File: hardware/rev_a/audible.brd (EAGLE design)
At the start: 27.7 x 23.4 mm, 28 parts, among them IC1 LTC1966CMS8, J1 SQUALL_HEADER, J5 TC2030-JLINK-NL, Q1 FK3503010L, U1 MAX417ESA+, U2 MAX417ESA+, U3 LD39015, U4 ICS-40310

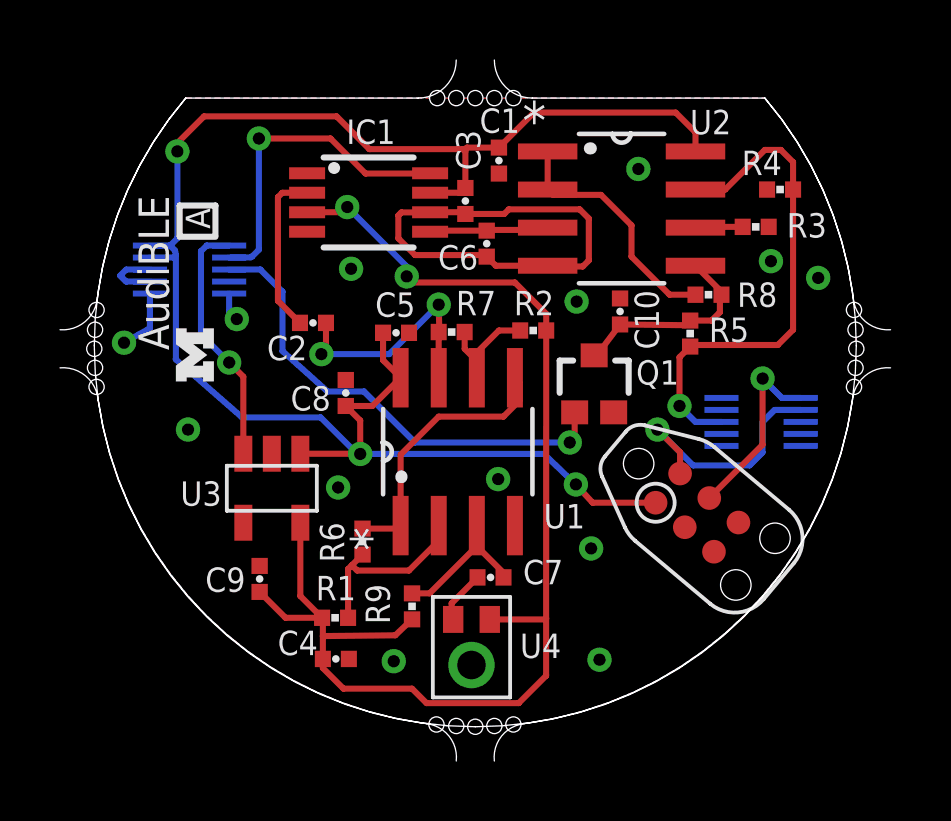
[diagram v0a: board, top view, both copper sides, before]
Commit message: Updated Part Names and digikey part names
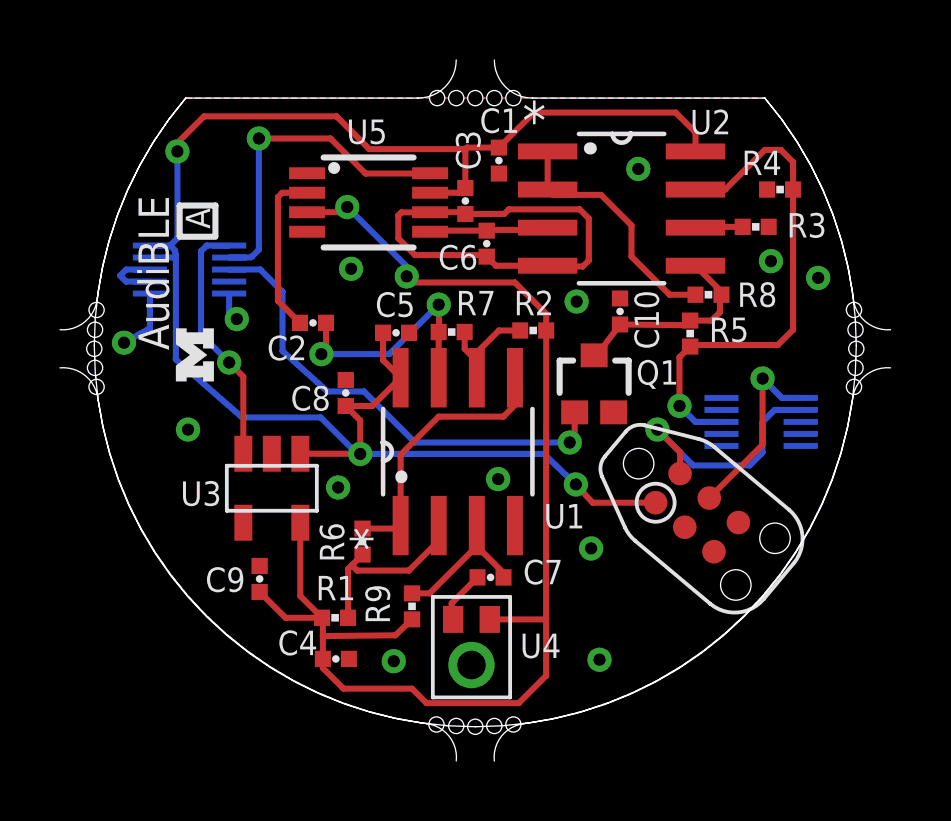
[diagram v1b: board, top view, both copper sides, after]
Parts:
- renumbered IC1 to U5, J5 to J2
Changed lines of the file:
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@@
 <grid distance="0.1" unitdist="mil" unit="mil" style="lines" multiple="1" display="yes" altdistance="0.01" altunitdist="inch" altunit="inch"/>
 <layers>
-<layer number="1" name="Top" color="4" fill="1" visible="no" active="yes"/>
+<layer number="1" name="Top" color="4" fill="1" visible="yes" active="yes"/>
 <layer number="2" name="Route2" color="1" fill="3" visible="no" active="no"/>
 <layer number="3" name="Route3" color="4" fill="3" visible="no" active="no"/>
@@
 <layer number="18" name="Vias" color="2" fill="1" visible="yes" active="yes"/>
 <layer number="19" name="Unrouted" color="13" fill="1" visible="yes" active="yes"/>
-<layer number="20" name="Dimension" color="15" fill="1" visible="no" active="yes"/>
-<layer number="21" name="tPlace" color="7" fill="1" visible="no" active="yes"/>
+<layer number="20" name="Dimension" color="15" fill="1" visible="yes" active="yes"/>
+<layer number="21" name="tPlace" color="7" fill="1" visible="yes" active="yes"/>
 <layer number="22" name="bPlace" color="7" fill="1" visible="yes" active="yes"/>
-<layer number="23" name="tOrigins" color="15" fill="1" visible="no" active="yes"/>
-<layer number="24" name="bOrigins" color="15" fill="1" visible="no" active="yes"/>
-<layer number="25" name="tNames" color="7" fill="1" visible="no" active="yes"/>
+<layer number="23" name="tOrigins" color="15" fill="1" visible="yes" active="yes"/>
+<layer number="24" name="bOrigins" color="15" fill="1" visible="yes" active="yes"/>
+<layer number="25" name="tNames" color="7" fill="1" visible="yes" active="yes"/>
 <layer number="26" name="bNames" color="7" fill="1" visible="yes" active="yes"/>
 <layer number="27" name="tValues" color="7" fill="1" visible="no" active="yes"/>
@@
 <layer number="49" name="Reference" color="7" fill="1" visible="no" active="yes"/>
 <layer number="50" name="dxf" color="7" fill="1" visible="no" active="no"/>
-<layer number="51" name="tDocu" color="6" fill="1" visible="no" active="yes"/>
-<layer number="52" name="bDocu" color="6" fill="1" visible="no" active="yes"/>
+<layer number="51" name="tDocu" color="6" fill="1" visible="yes" active="yes"/>
+<layer number="52" name="bDocu" color="6" fill="1" visible="yes" active="yes"/>
 <layer number="53" name="tGND_GNDA" color="7" fill="9" visible="no" active="no"/>
 <layer number="54" name="bGND_GNDA" color="1" fill="9" visible="no" active="no"/>
@@
 </element>
 <element name="U$1" library="logos" package="UMICH_SOLID_50MIL" value="" x="14.7828" y="12.3952" smashed="yes" rot="R90"/>
-<element name="J5" library="connector" package="TC2030-IDC-NL" value="TC2030-JLINK-NL" x="31.5214" y="7.1374" smashed="yes" rot="R320">
+<element name="J2" library="connector" package="TC2030-IDC-NL" value="TC2030-JLINK-NL" x="31.5214" y="7.1374" smashed="yes" rot="R320">
 <attribute name="VALUE" x="29.2764625" y="4.4619875" size="1.016" layer="27" font="vector" ratio="12" rot="R320" align="bottom-center"/>
 </element>
@@
 </element>
 <element name="U4" library="chips" package="LGA_CAV3" value="ICS-40310" x="24.003" y="2.0574" smashed="yes" rot="R270"/>
-<element name="IC1" library="chips" package="MSOP8" value="LTC1966CMS8" x="20.574" y="17.4752" smashed="yes" rot="R270">
+<element name="U5" library="chips" package="MSOP8" value="LTC1966CMS8" x="20.574" y="17.4752" smashed="yes" rot="R270">
 <attribute name="NAME" x="19.832" y="19.4278" size="0.8128" layer="25"/>
 <attribute name="VALUE" x="18.962" y="14.6472" size="1.016" layer="27"/>
@@
 <contactref element="J1" pad="A1"/>
 <contactref element="J1" pad="A3"/>
-<contactref element="J5" pad="1"/>
+<contactref element="J2" pad="1"/>
 <contactref element="C8" pad="1"/>
-<contactref element="IC1" pad="7"/>
+<contactref element="U5" pad="7"/>
 <contactref element="U1" pad="8"/>
 <contactref element="U2" pad="8"/>
@@
 <vertex x="33.782" y="20.955" curve="-40.54"/>
 </polygon>
-<contactref element="J5" pad="5"/>
+<contactref element="J2" pad="5"/>
 <contactref element="C8" pad="2"/>
 <contactref element="U2" pad="4"/>
-<contactref element="IC1" pad="1"/>
-<contactref element="IC1" pad="4"/>
+<contactref element="U5" pad="1"/>
+<contactref element="U5" pad="4"/>
 <contactref element="C9" pad="2"/>
 <contactref element="U4" pad="P$2"/>
@@
 <contactref element="C3" pad="1"/>
 <contactref element="C6" pad="1"/>
-<contactref element="IC1" pad="6"/>
+<contactref element="U5" pad="6"/>
 <wire x1="23.7998" y1="17.09293125" x2="25.09393125" y2="17.09293125" width="0.2032" layer="1"/>
 <wire x1="25.0698" y1="18.28673125" x2="24.9174" y2="18.43913125" width="0.2032" layer="1"/>
@@
 <signal name="P23">
 <contactref element="J1" pad="A4"/>
-<contactref element="IC1" pad="8"/>
+<contactref element="U5" pad="8"/>
 <via x="16.9164" y="19.6088" extent="1-16" drill="0.4064"/>
 <wire x1="16.9164" y1="19.6088" x2="16.9164" y2="15.9004" width="0.2032" layer="16"/>
@@
 <signal name="SWDCLK">
 <contactref element="J1" pad="B2"/>
-<contactref element="J5" pad="4"/>
+<contactref element="J2" pad="4"/>
 <via x="33.7058" y="11.6078" extent="1-16" drill="0.4064"/>
 <wire x1="33.7058" y1="11.6078" x2="34.3536" y2="10.96" width="0.2032" layer="16"/>
@@
 <signal name="SWDIO/!RESET">
 <contactref element="J1" pad="B4"/>
-<contactref element="J5" pad="2"/>
+<contactref element="J2" pad="2"/>
 <via x="30.2006" y="9.906" extent="1-16" drill="0.4064"/>
 <wire x1="30.2006" y1="9.906" x2="31.3944" y2="8.7122" width="0.2032" layer="16"/>
@@
 <contactref element="U4" pad="P$3"/>
 <contactref element="R2" pad="2"/>
-<contactref element="IC1" pad="3"/>
+<contactref element="U5" pad="3"/>
 <contactref element="C4" pad="1"/>
 <contactref element="U3" pad="5"/>
@@
 </signal>
 <signal name="N$2">
-<contactref element="IC1" pad="2"/>
+<contactref element="U5" pad="2"/>
 <contactref element="C2" pad="2"/>
 <wire x1="18.524" y1="17.8002" x2="17.6986" y2="17.8002" width="0.2032" layer="1"/>
@@
 <signal name="N$3">
 <contactref element="U2" pad="3"/>
-<contactref element="IC1" pad="5"/>
+<contactref element="U5" pad="5"/>
 <contactref element="C6" pad="2"/>
 <wire x1="25.80766875" y1="16.5608" x2="26.543" y2="16.637" width="0.2032" layer="1"/>
